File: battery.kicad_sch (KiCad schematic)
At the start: 29 parts, among them J4 S2B-PH-SM4-TB_LF__SN_, U10 MAX17048G+T10, U11 MP2637GR-P

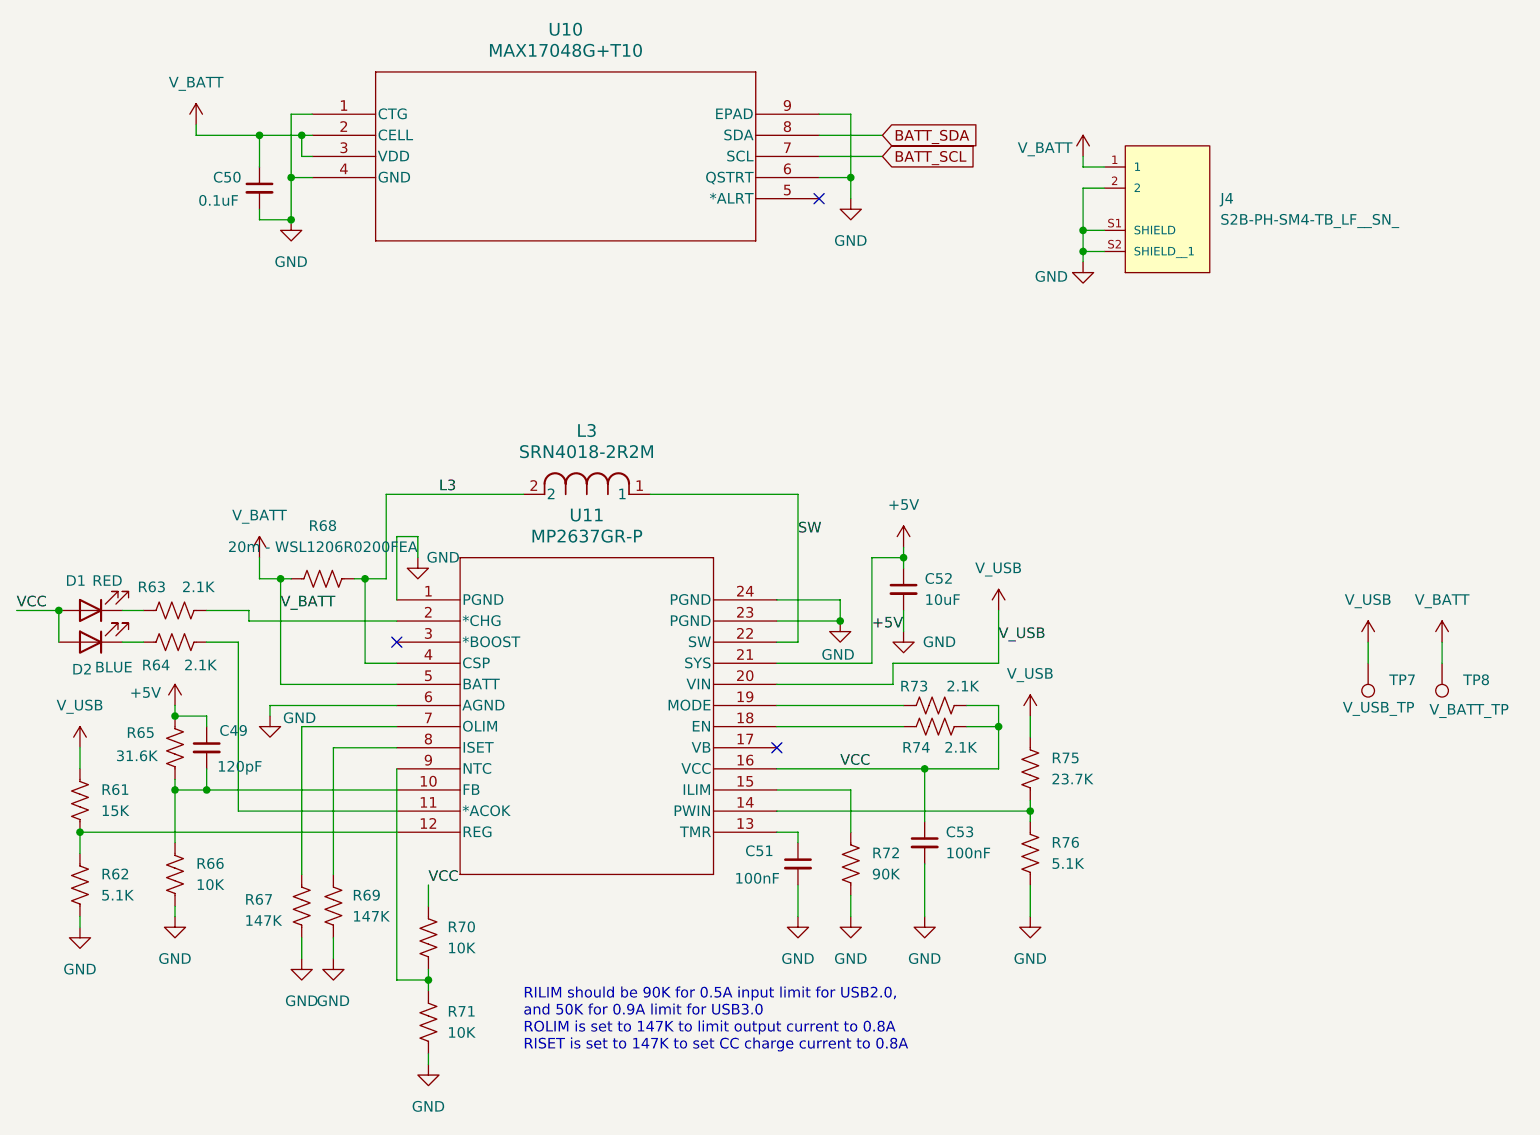
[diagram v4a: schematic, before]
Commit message: Replaced all passive footprints from 0603 metric to 0603 imperial. Big oversight. All done. Next is DRC
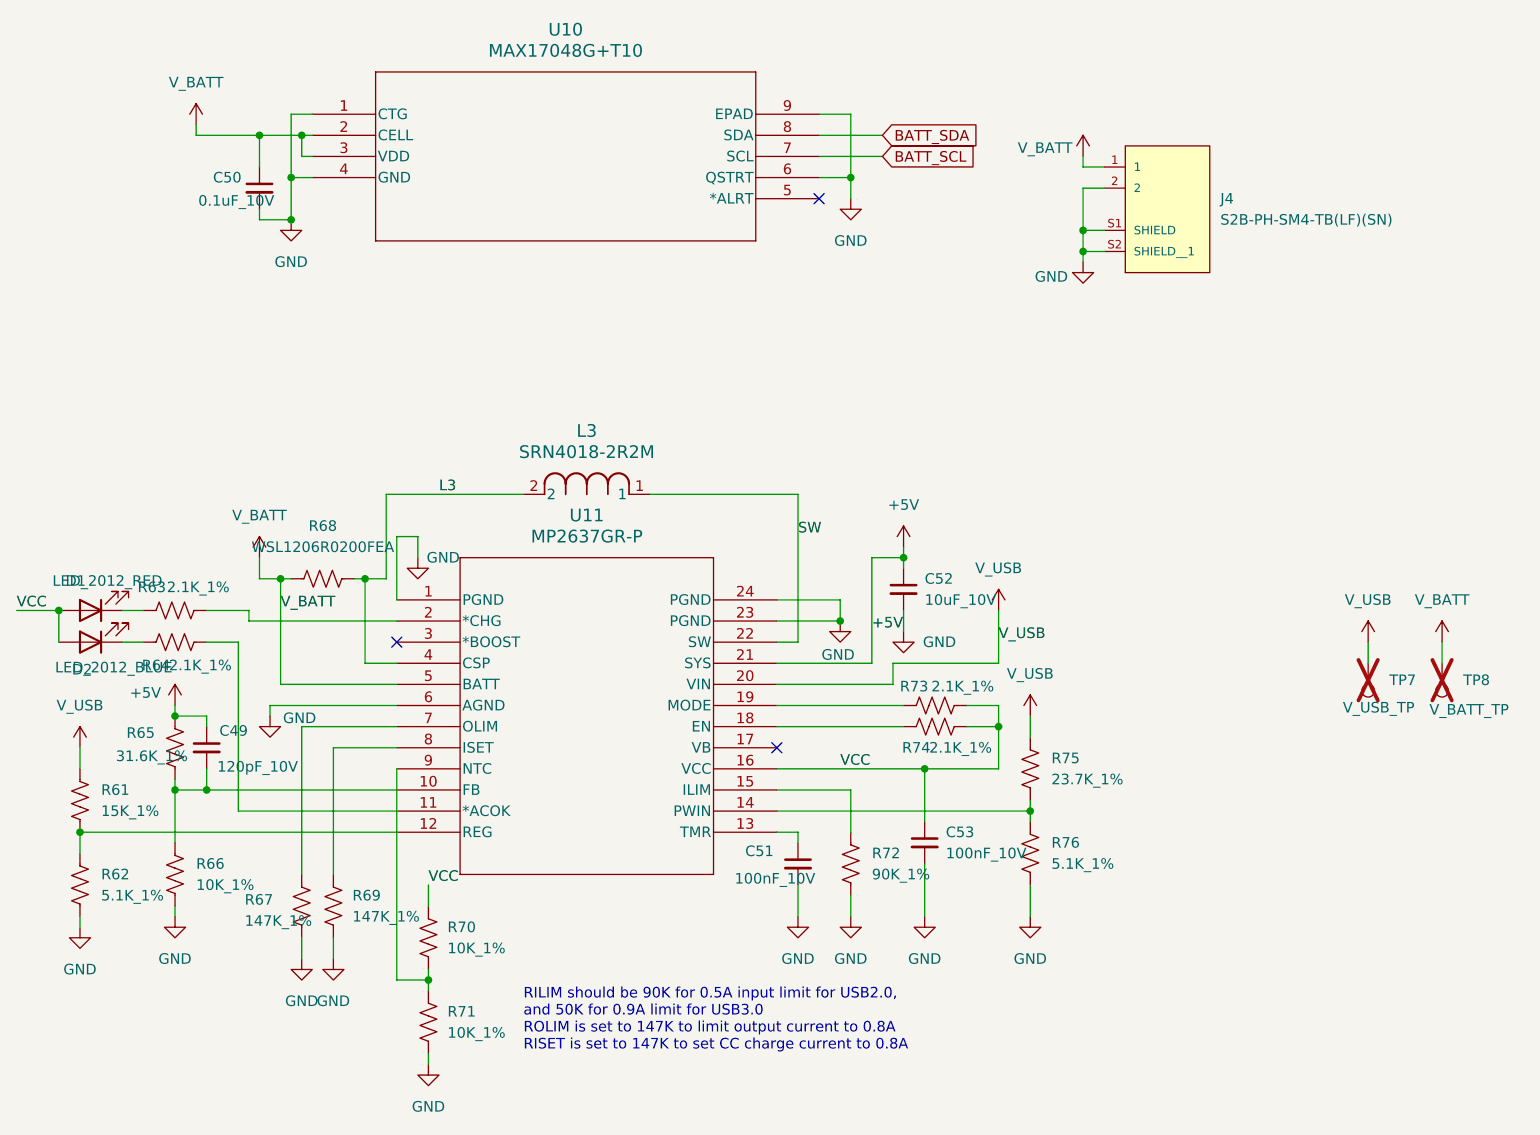
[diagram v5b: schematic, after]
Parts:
- C49: value 120pF -> 120pF_10V; footprint Capacitor_SMD:C_0201_0603Metric_Pad0.64x0.40mm_HandSolder -> Capacitor_SMD:C_0603_1608Metric
- C50: value 0.1uF -> 0.1uF_10V; footprint Capacitor_SMD:C_0201_0603Metric_Pad0.64x0.40mm_HandSolder -> Capacitor_SMD:C_0603_1608Metric
- C51, C53: value 100nF -> 100nF_10V; footprint Capacitor_SMD:C_0201_0603Metric_Pad0.64x0.40mm_HandSolder -> Capacitor_SMD:C_0603_1608Metric
- C52: value 10uF -> 10uF_10V; footprint Capacitor_SMD:C_0201_0603Metric_Pad0.64x0.40mm_HandSolder -> Capacitor_SMD:C_0603_1608Metric
- D1: value RED -> LED_2012_RED
- D2: value BLUE -> LED_2012_BLUE
- J4: value S2B-PH-SM4-TB_LF__SN_ -> S2B-PH-SM4-TB(LF)(SN)
- R61: value 15K -> 15K_1%; footprint Resistor_SMD:R_0201_0603Metric_Pad0.64x0.40mm_HandSolder -> Resistor_SMD:R_0603_1608Metric
- R62, R76: value 5.1K -> 5.1K_1%; footprint Resistor_SMD:R_0201_0603Metric_Pad0.64x0.40mm_HandSolder -> Resistor_SMD:R_0603_1608Metric
- R63, R64, R73, R74: value 2.1K -> 2.1K_1%; footprint Resistor_SMD:R_0201_0603Metric_Pad0.64x0.40mm_HandSolder -> Resistor_SMD:R_0603_1608Metric
- R65: value 31.6K -> 31.6K_1%; footprint Resistor_SMD:R_0201_0603Metric_Pad0.64x0.40mm_HandSolder -> Resistor_SMD:R_0603_1608Metric
- R66, R70, R71: value 10K -> 10K_1%; footprint Resistor_SMD:R_0201_0603Metric_Pad0.64x0.40mm_HandSolder -> Resistor_SMD:R_0603_1608Metric
- R67, R69: value 147K -> 147K_1%; footprint Resistor_SMD:R_0201_0603Metric_Pad0.64x0.40mm_HandSolder -> Resistor_SMD:R_0603_1608Metric
- R68: value 20m - WSL1206R0200FEA -> WSL1206R0200FEA
- R72: value 90K -> 90K_1%; footprint Resistor_SMD:R_0201_0603Metric_Pad0.64x0.40mm_HandSolder -> Resistor_SMD:R_0603_1608Metric
- R75: value 23.7K -> 23.7K_1%; footprint Resistor_SMD:R_0201_0603Metric_Pad0.64x0.40mm_HandSolder -> Resistor_SMD:R_0603_1608Metric
- TP7, TP8: now not fitted
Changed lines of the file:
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@@
 			)
 		)
-		(property "Value" "10K"
+		(property "Value" "10K_1%"
 			(at 67.056 137.16 0)
 			(effects
@@
 			)
 		)
-		(property "Footprint" "Resistor_SMD:R_0201_0603Metric_Pad0.64x0.40mm_HandSolder"
+		(property "Footprint" "Resistor_SMD:R_0603_1608Metric"
 			(at 65.786 136.144 90)
 			(effects
@@
 			)
 		)
-		(property "Value" "2.1K"
+		(property "Value" "2.1K_1%"
 			(at 128.778 113.03 90)
 			(effects
@@
 			)
 		)
-		(property "Footprint" "Resistor_SMD:R_0201_0603Metric_Pad0.64x0.40mm_HandSolder"
+		(property "Footprint" "Resistor_SMD:R_0603_1608Metric"
 			(at 125.984 109.474 90)
 			(effects
@@
 			)
 		)
-		(property "Value" "0.1uF"
+		(property "Value" "0.1uF_10V"
 			(at 37.084 47.244 0)
 			(effects
@@
 			)
 		)
-		(property "Footprint" "Capacitor_SMD:C_0201_0603Metric_Pad0.64x0.40mm_HandSolder"
+		(property "Footprint" "Capacitor_SMD:C_0603_1608Metric"
 			(at 44.45 45.72 0)
 			(effects
@@
 			)
 		)
-		(property "Value" "120pF"
+		(property "Value" "120pF_10V"
 			(at 39.37 115.316 0)
 			(effects
@@
 			)
 		)
-		(property "Footprint" "Capacitor_SMD:C_0201_0603Metric_Pad0.64x0.40mm_HandSolder"
+		(property "Footprint" "Capacitor_SMD:C_0603_1608Metric"
 			(at 38.1 113.03 0)
 			(effects
@@
 			)
 		)
-		(property "Value" "10uF"
+		(property "Value" "10uF_10V"
 			(at 124.46 95.2562 0)
 			(effects
@@
 			)
 		)
-		(property "Footprint" "Capacitor_SMD:C_0201_0603Metric_Pad0.64x0.40mm_HandSolder"
+		(property "Footprint" "Capacitor_SMD:C_0603_1608Metric"
 			(at 121.92 93.98 0)
 			(effects
@@
 			)
 		)
-		(property "Value" "23.7K"
+		(property "Value" "23.7K_1%"
 			(at 139.7 116.8399 0)
 			(effects
@@
 			)
 		)
-		(property "Footprint" "Resistor_SMD:R_0201_0603Metric_Pad0.64x0.40mm_HandSolder"
+		(property "Footprint" "Resistor_SMD:R_0603_1608Metric"
 			(at 138.176 115.824 90)
 			(effects
@@
 			)
 		)
-		(property "Value" "10K"
+		(property "Value" "10K_1%"
 			(at 36.83 129.5399 0)
 			(effects
@@
 			)
 		)
-		(property "Footprint" "Resistor_SMD:R_0201_0603Metric_Pad0.64x0.40mm_HandSolder"
+		(property "Footprint" "Resistor_SMD:R_0603_1608Metric"
 			(at 35.306 128.524 90)
 			(effects
@@
 			)
 		)
-		(property "Value" "RED"
+		(property "Value" "LED_2012_RED"
 			(at 26.162 92.964 0)
 			(effects
@@
 			)
 		)
-		(property "Value" "90K"
+		(property "Value" "90K_1%"
 			(at 118.11 128.2699 0)
 			(effects
@@
 			)
 		)
-		(property "Footprint" "Resistor_SMD:R_0201_0603Metric_Pad0.64x0.40mm_HandSolder"
+		(property "Footprint" "Resistor_SMD:R_0603_1608Metric"
 			(at 116.586 127.254 90)
 			(effects
@@
 			)
 		)
-		(property "Value" "2.1K"
+		(property "Value" "2.1K_1%"
 			(at 37.084 93.726 90)
 			(effects
@@
 			)
 		)
-		(property "Footprint" "Resistor_SMD:R_0201_0603Metric_Pad0.64x0.40mm_HandSolder"
+		(property "Footprint" "Resistor_SMD:R_0603_1608Metric"
 			(at 34.544 95.504 90)
 			(effects
@@
 			)
 		)
-		(property "Value" "5.1K"
+		(property "Value" "5.1K_1%"
 			(at 139.7 126.9999 0)
 			(effects
@@
 			)
 		)
-		(property "Footprint" "Resistor_SMD:R_0201_0603Metric_Pad0.64x0.40mm_HandSolder"
+		(property "Footprint" "Resistor_SMD:R_0603_1608Metric"
 			(at 138.176 125.984 90)
 			(effects
@@
 			)
 		)
-		(property "Value" "147K"
+		(property "Value" "147K_1%"
 			(at 42.672 133.858 0)
 			(effects
@@
 			)
 		)
-		(property "Footprint" "Resistor_SMD:R_0201_0603Metric_Pad0.64x0.40mm_HandSolder"
+		(property "Footprint" "Resistor_SMD:R_0603_1608Metric"
 			(at 50.546 132.334 90)
 			(effects
@@
 			)
 		)
-		(property "Value" "100nF"
+		(property "Value" "100nF_10V"
 			(at 101.6 128.778 0)
 			(effects
@@
 			)
 		)
-		(property "Footprint" "Capacitor_SMD:C_0201_0603Metric_Pad0.64x0.40mm_HandSolder"
+		(property "Footprint" "Capacitor_SMD:C_0603_1608Metric"
 			(at 109.22 127 0)
 			(effects
@@
 			)
 		)
-		(property "Value" "15K"
+		(property "Value" "15K_1%"
 			(at 25.4 120.6499 0)
 			(effects
@@
 			)
 		)
-		(property "Footprint" "Resistor_SMD:R_0201_0603Metric_Pad0.64x0.40mm_HandSolder"
+		(property "Footprint" "Resistor_SMD:R_0603_1608Metric"
 			(at 23.876 119.634 90)
 			(effects
@@
 			)
 		)
-		(property "Value" "2.1K"
+		(property "Value" "2.1K_1%"
 			(at 37.338 103.124 90)
 			(effects
@@
 			)
 		)
-		(property "Footprint" "Resistor_SMD:R_0201_0603Metric_Pad0.64x0.40mm_HandSolder"
+		(property "Footprint" "Resistor_SMD:R_0603_1608Metric"
 			(at 34.544 99.314 90)
 			(effects
@@
 			)
 		)
-		(property "Value" "147K"
+		(property "Value" "147K_1%"
 			(at 55.626 133.35 0)
 			(effects
@@
 			)
 		)
-		(property "Footprint" "Resistor_SMD:R_0201_0603Metric_Pad0.64x0.40mm_HandSolder"
+		(property "Footprint" "Resistor_SMD:R_0603_1608Metric"
 			(at 54.356 132.334 90)
 			(effects
@@
 			)
 		)
-		(property "Value" "20m - WSL1206R0200FEA"
+		(property "Value" "WSL1206R0200FEA"
 			(at 52.07 88.9 90)
 			(effects
@@
 		(in_bom yes)
 		(on_board yes)
-		(dnp no)
+		(dnp yes)
 		(property "Reference" "TP7"
 			(at 180.34 104.9019 0)
@@
 			)
 		)
-		(property "Value" "31.6K"
+		(property "Value" "31.6K_1%"
 			(at 27.178 114.046 0)
 			(effects
@@
 			)
 		)
-		(property "Footprint" "Resistor_SMD:R_0201_0603Metric_Pad0.64x0.40mm_HandSolder"
+		(property "Footprint" "Resistor_SMD:R_0603_1608Metric"
 			(at 35.306 113.284 90)
 			(effects
@@
 			)
 		)
-		(property "Value" "5.1K"
+		(property "Value" "5.1K_1%"
 			(at 25.4 130.8099 0)
 			(effects
@@
 			)
 		)
-		(property "Footprint" "Resistor_SMD:R_0201_0603Metric_Pad0.64x0.40mm_HandSolder"
+		(property "Footprint" "Resistor_SMD:R_0603_1608Metric"
 			(at 23.876 129.794 90)
 			(effects
@@
 		(in_bom yes)
 		(on_board yes)
-		(dnp no)
+		(dnp yes)
 		(property "Reference" "TP8"
 			(at 189.23 104.9019 0)
@@
 			)
 		)
-		(property "Value" "S2B-PH-SM4-TB_LF__SN_"
+		(property "Value" "S2B-PH-SM4-TB(LF)(SN)"
 			(at 160.02 49.5299 0)
 			(effects
@@
 			)
 		)
-		(property "Value" "BLUE"
+		(property "Value" "LED_2012_BLUE"
 			(at 26.924 103.378 0)
 			(effects
@@
 			)
 		)
-		(property "Value" "10K"
+		(property "Value" "10K_1%"
 			(at 67.056 147.32 0)
 			(effects
@@
 			)
 		)
-		(property "Footprint" "Resistor_SMD:R_0201_0603Metric_Pad0.64x0.40mm_HandSolder"
+		(property "Footprint" "Resistor_SMD:R_0603_1608Metric"
 			(at 65.786 146.304 90)
 			(effects
@@
 			)
 		)
-		(property "Value" "100nF"
+		(property "Value" "100nF_10V"
 			(at 127 125.7362 0)
 			(effects
@@
 			)
 		)
-		(property "Footprint" "Capacitor_SMD:C_0201_0603Metric_Pad0.64x0.40mm_HandSolder"
+		(property "Footprint" "Capacitor_SMD:C_0603_1608Metric"
 			(at 124.46 124.46 0)
 			(effects
@@
 			)
 		)
-		(property "Value" "2.1K"
+		(property "Value" "2.1K_1%"
 			(at 129.032 105.664 90)
 			(effects
@@
 			)
 		)
-		(property "Footprint" "Resistor_SMD:R_0201_0603Metric_Pad0.64x0.40mm_HandSolder"
+		(property "Footprint" "Resistor_SMD:R_0603_1608Metric"
 			(at 125.476 108.966 90)
 			(effects

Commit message: All fiducials and mounting holes placed. Except one hole, which I'll try to place. WIP
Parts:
- L3: footprint IND_BOURNS_SRN4018 -> SRN4018-2R2M:IND_BOURNS_SRN4018
- U10: footprint 21-0168E_T822-3_MXM -> MAX17048G-T10:21-0168E_T822-3_MXM
- U11: footprint QFN-24_MP2637_MNP -> MP2637:QFN-24_MP2637_MNP
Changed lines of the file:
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@@
 			)
 		)
-		(property "Footprint" "IND_BOURNS_SRN4018"
+		(property "Footprint" "SRN4018-2R2M:IND_BOURNS_SRN4018"
 			(at 76.2 82.55 0)
 			(effects
@@
 			)
 		)
-		(property "Footprint" "21-0168E_T822-3_MXM"
+		(property "Footprint" "MAX17048G-T10:21-0168E_T822-3_MXM"
 			(at 50.8 36.83 0)
 			(effects
@@
 			)
 		)
-		(property "Footprint" "QFN-24_MP2637_MNP"
+		(property "Footprint" "MP2637:QFN-24_MP2637_MNP"
 			(at 60.96 95.25 0)
 			(effects

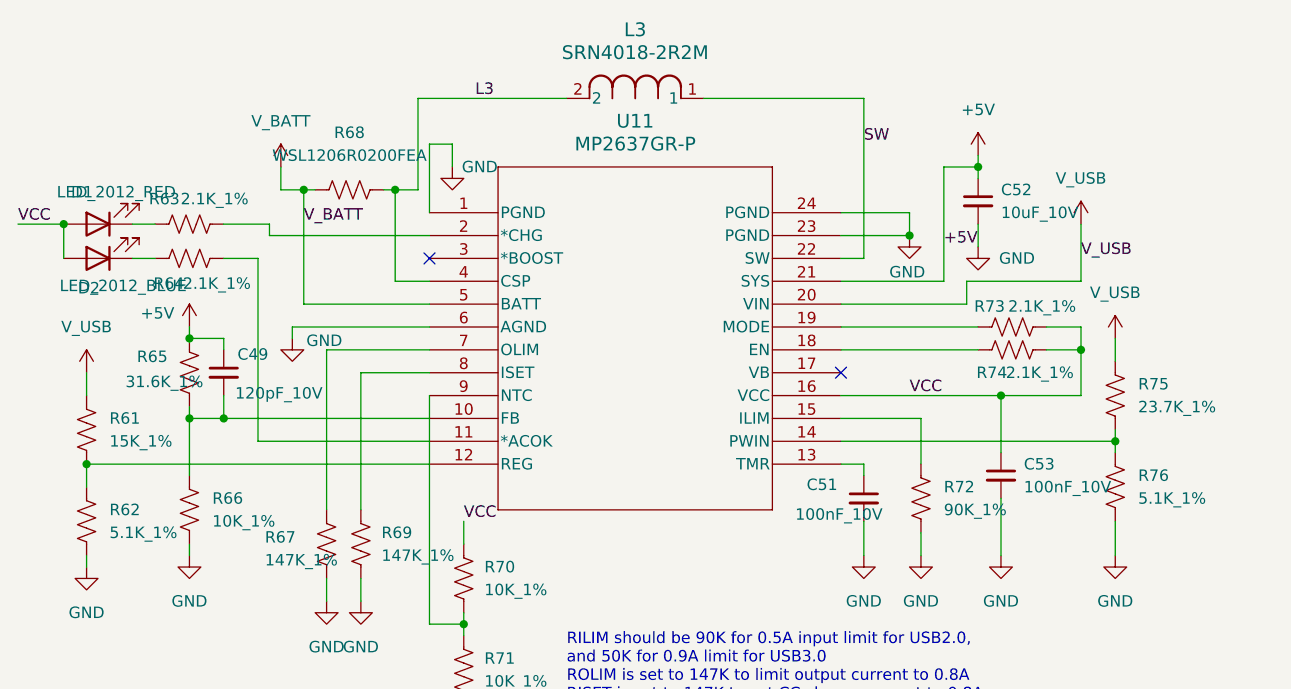
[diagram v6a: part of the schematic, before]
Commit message: Updated LED footprint to 0603, which was easier to find
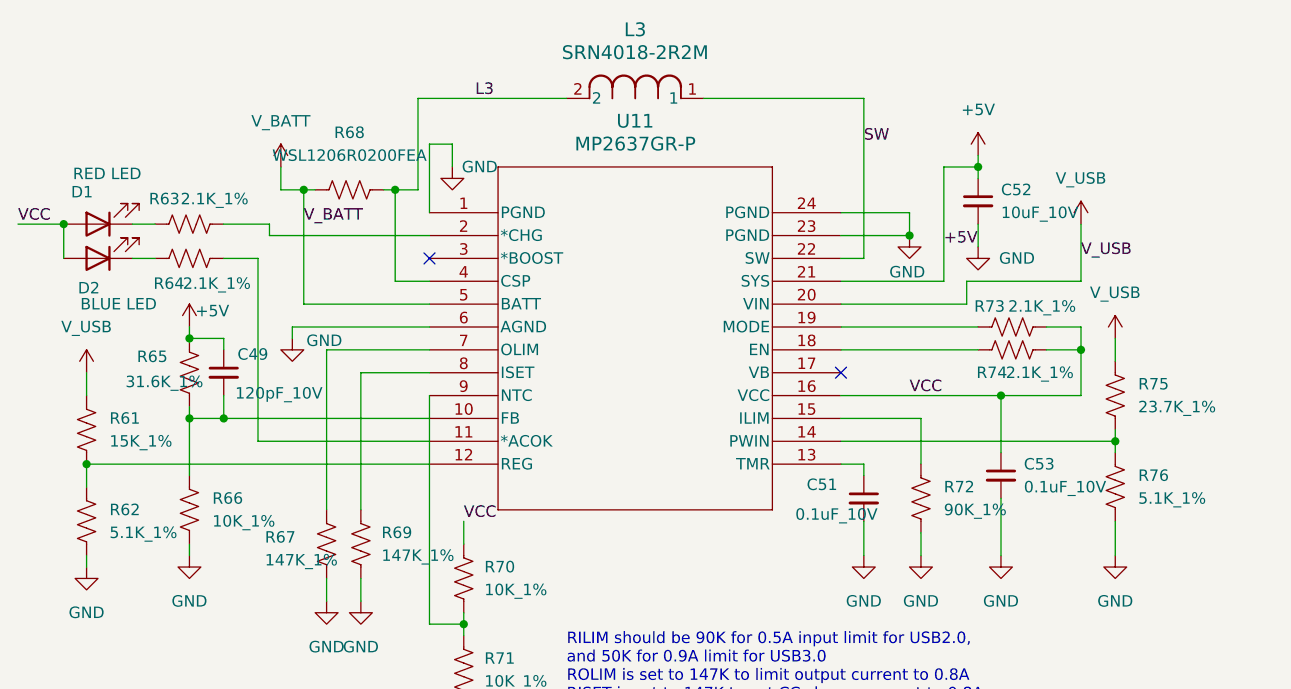
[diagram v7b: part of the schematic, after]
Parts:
- C51, C53: value 100nF_10V -> 0.1uF_10V
- D1: value LED_2012_RED -> RED LED; footprint LED_SMD:LED_0805_2012Metric -> LED_SMD:LED_0603_1608Metric
- D2: value LED_2012_BLUE -> BLUE LED; footprint LED_SMD:LED_0805_2012Metric -> LED_SMD:LED_0603_1608Metric
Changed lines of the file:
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@@
 			)
 		)
-		(property "Value" "LED_2012_RED"
-			(at 26.162 92.964 0)
-			(effects
-				(font
-					(size 1.27 1.27)
-				)
-			)
-		)
-		(property "Footprint" "LED_SMD:LED_0805_2012Metric"
+		(property "Value" "RED LED"
+			(at 25.146 90.932 0)
+			(effects
+				(font
+					(size 1.27 1.27)
+				)
+			)
+		)
+		(property "Footprint" "LED_SMD:LED_0603_1608Metric"
 			(at 24.13 96.52 0)
 			(effects
@@
 			)
 		)
-		(property "Value" "100nF_10V"
+		(property "Value" "0.1uF_10V"
 			(at 101.6 128.778 0)
 			(effects
@@
 			)
 		)
-		(property "Value" "LED_2012_BLUE"
-			(at 26.924 103.378 0)
-			(effects
-				(font
-					(size 1.27 1.27)
-				)
-			)
-		)
-		(property "Footprint" "LED_SMD:LED_0805_2012Metric"
+		(property "Value" "BLUE LED"
+			(at 26.416 105.41 0)
+			(effects
+				(font
+					(size 1.27 1.27)
+				)
+			)
+		)
+		(property "Footprint" "LED_SMD:LED_0603_1608Metric"
 			(at 24.13 100.33 0)
 			(effects
@@
 		)
 		(property "Value" "+5V"
-			(at 30.734 106.426 0)
+			(at 36.83 106.172 0)
 			(effects
 				(font
@@
 			)
 		)
-		(property "Value" "100nF_10V"
+		(property "Value" "0.1uF_10V"
 			(at 127 125.7362 0)
 			(effects
